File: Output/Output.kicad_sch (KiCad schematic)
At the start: 8 parts, among them J1 Conn_01x10_Pin, J2 Conn_01x04_Pin, J3 Conn_01x03_Pin, J4 Conn_01x02_Pin, J5 Conn_01x01_Pin, U2 74LS273

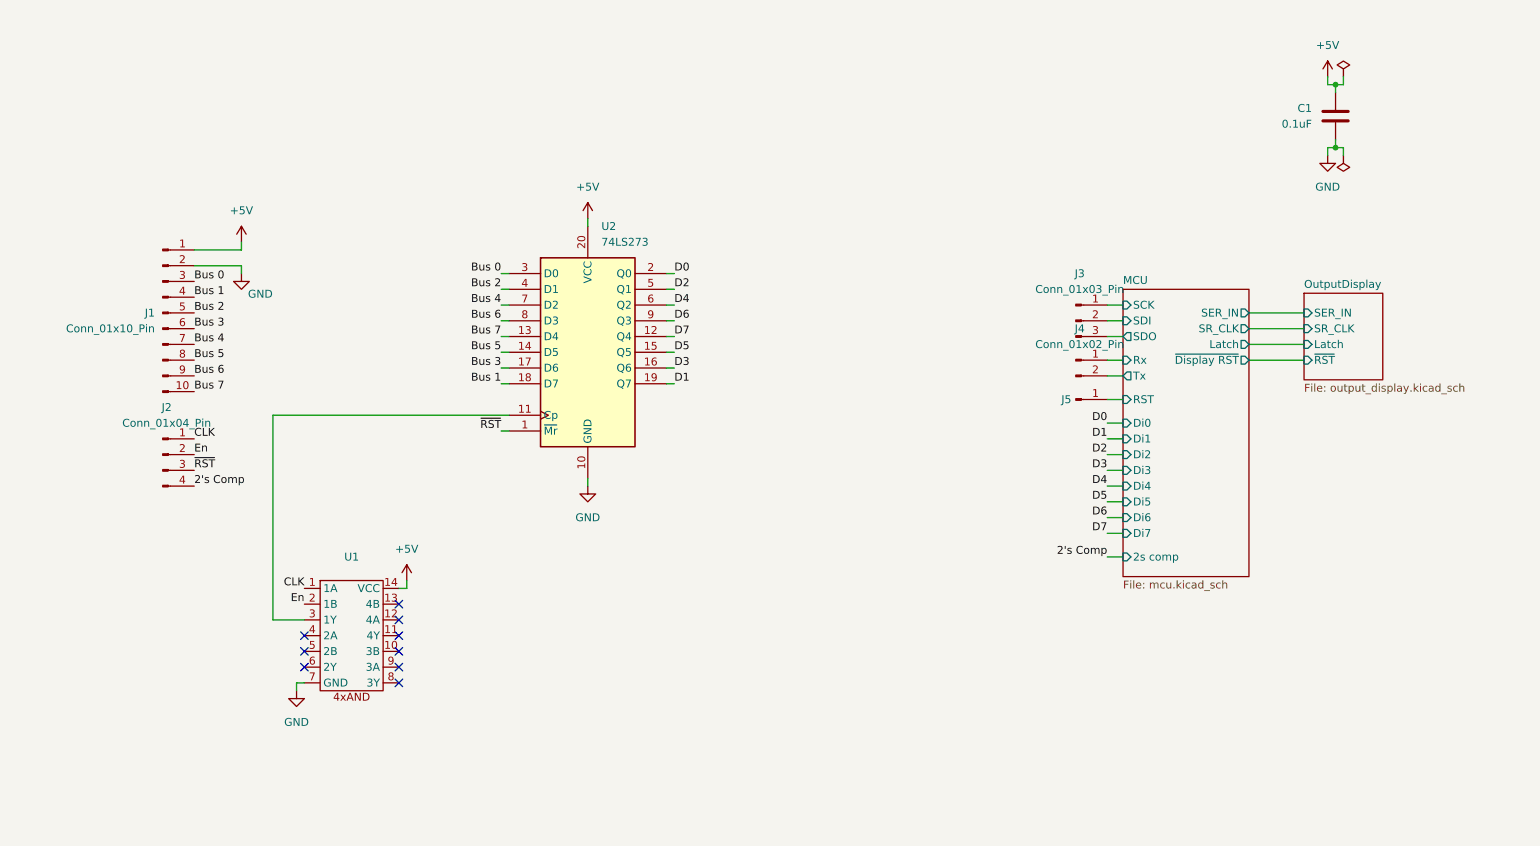
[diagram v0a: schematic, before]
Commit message: Updated output to use 2 4-bit registers instead of 1 8-bit because that's what I have. No longer need the AND for clk enable as registers have an enable pin. Enable is now active low. Reset is now active high
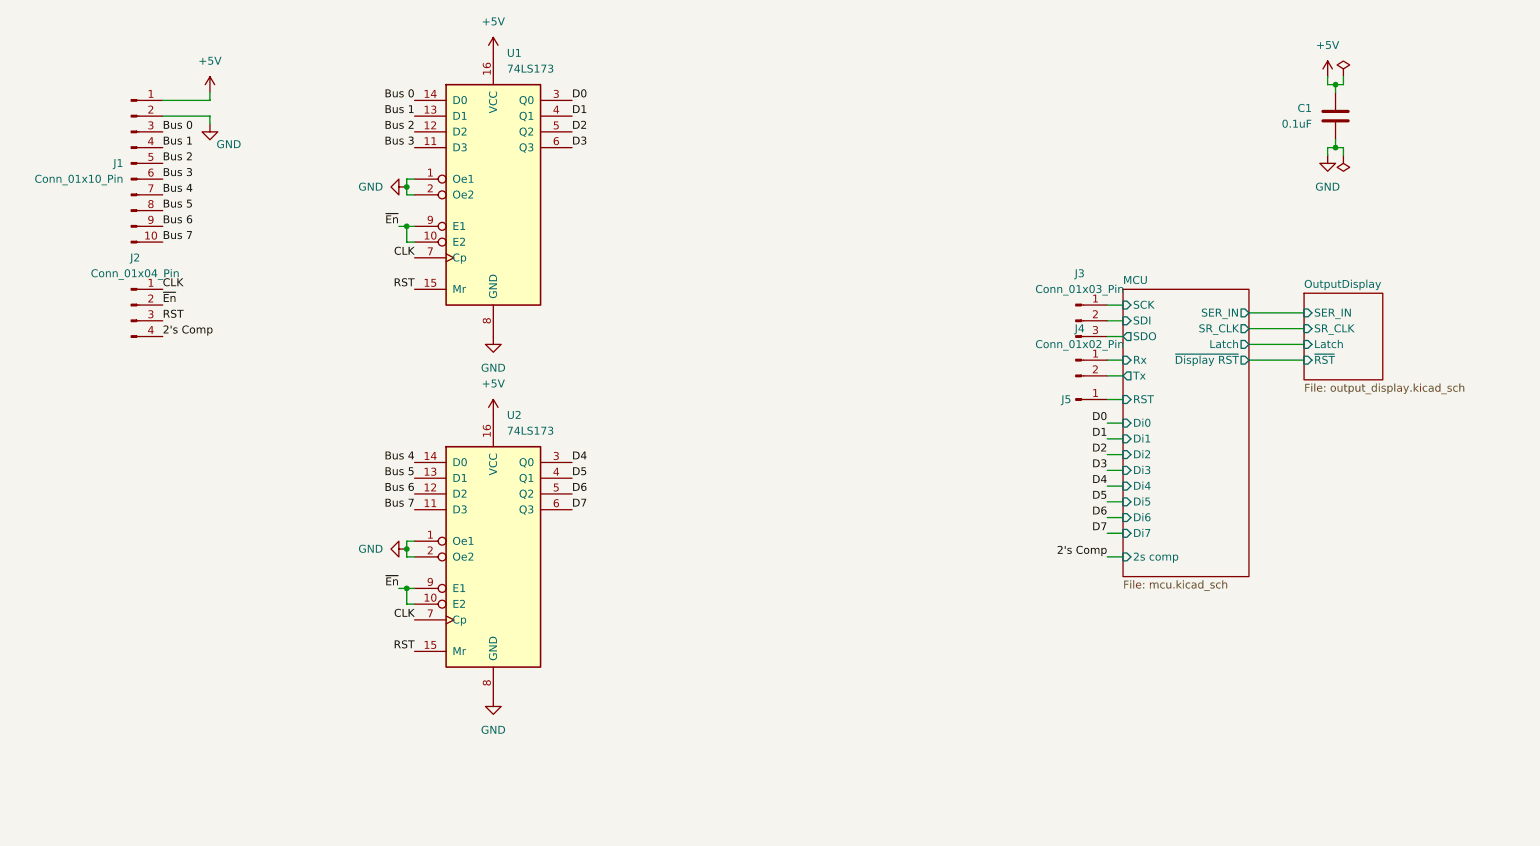
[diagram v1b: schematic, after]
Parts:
- removed U1: ~, 8BitCPUFootprints:4x_and, symbol 8BitCPU:4x_and
- removed U2: 74LS273, Package_DIP:DIP-20_W7.62mm, symbol 74xx:74LS273
- added U1, U2: 74LS173, symbol 74xx:74LS173
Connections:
- net +5V: now also U1.16 (VCC), U2.16 (VCC)
- net Bus 0: now also U1.14 (D0)
- net Bus 1: now also U1.13 (D1)
- net Bus 2: now also U1.12 (D2)
- net Bus 3: now also U1.11 (D3)
- net Bus 4: now also U2.14 (D0)
- net Bus 5: now also U2.13 (D1)
- net Bus 6: now also U2.12 (D2)
- net Bus 7: now also U2.11 (D3)
- net CLK: now also U1.7 (Cp), U2.7 (Cp)
- net D0: now also U1.3 (Q0)
- net D1: now also U1.4 (Q1)
- net D2: now also U1.5 (Q2)
- net D3: now also U1.6 (Q3)
- net D4: now also U2.3 (Q0)
- net D5: now also U2.4 (Q1)
- net D6: now also U2.5 (Q2)
- net D7: now also U2.6 (Q3)
- net GND: now also U1.1 (Oe1), U1.2 (Oe2), U1.8 (GND), U2.1 (Oe1), U2.2 (Oe2), U2.8 (GND)
- net En renamed ~{En}
- net ~{En}: now also U1.10 (E2), U1.9 (E1), U2.10 (E2), U2.9 (E1)
- net ~{RST} renamed RST
- net RST: now also U1.15 (Mr), U2.15 (Mr)
- no-connect marks 9 -> 0
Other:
- moved on the sheet: J1, J2

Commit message: Updated output to use eeprom and timing circuit instead of atmega a shift registers
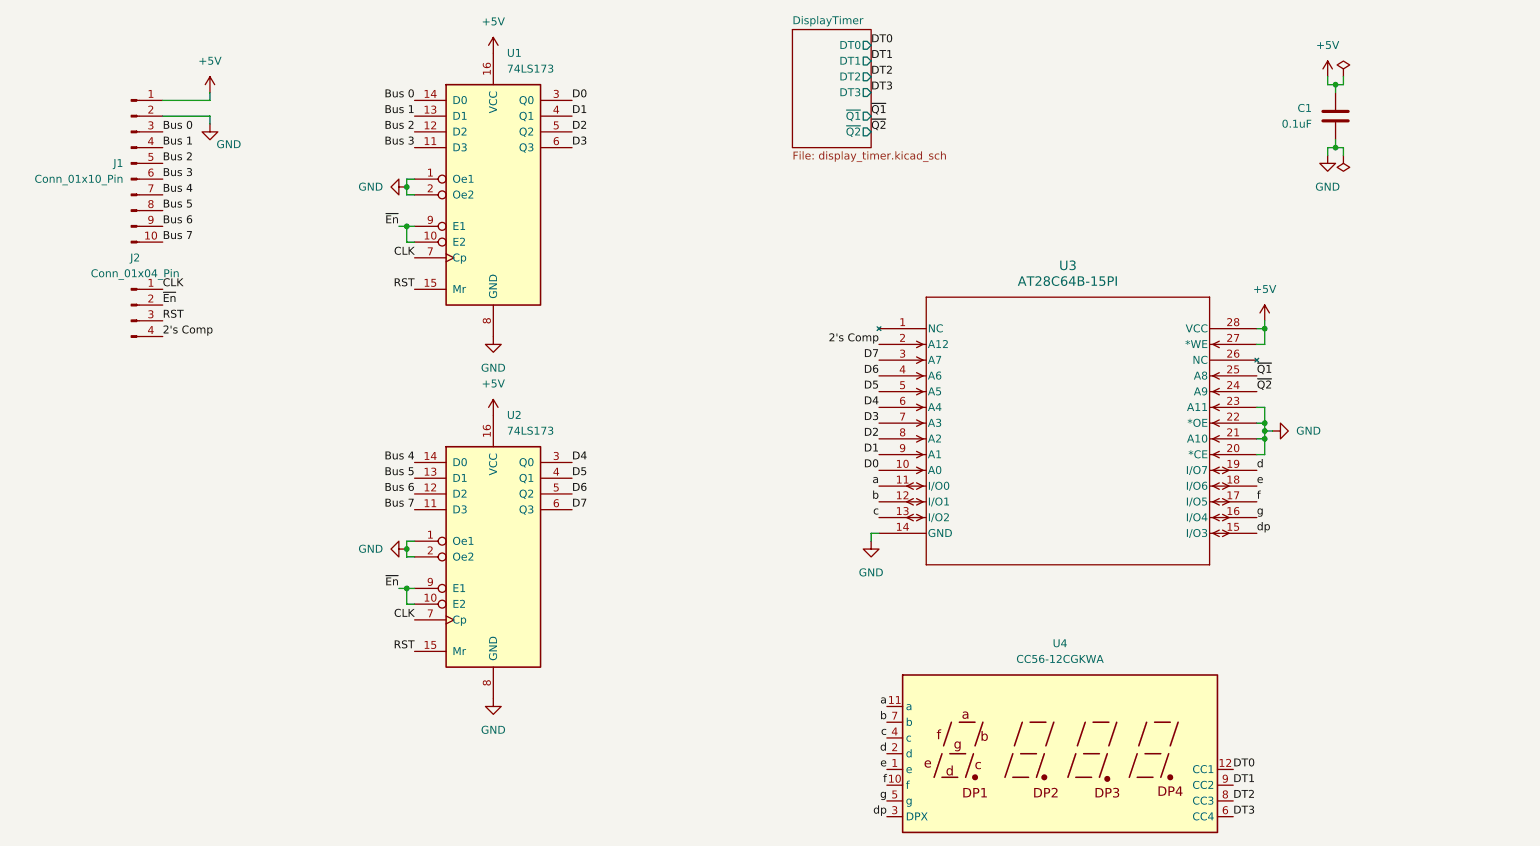
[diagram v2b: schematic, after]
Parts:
- removed J3: Conn_01x03_Pin, Connector_PinHeader_2.54mm:PinHeader_1x03_P2.54mm_Vertical, symbol Connector:Conn_01x03_Pin
- removed J4: Conn_01x02_Pin, Connector_PinHeader_2.54mm:PinHeader_1x02_P2.54mm_Vertical, symbol Connector:Conn_01x02_Pin
- removed J5: Conn_01x01_Pin, Connector_PinHeader_2.54mm:PinHeader_1x01_P2.54mm_Vertical, symbol Connector:Conn_01x01_Pin
- added U3: AT28C64B-15PI, 28P6, symbol eeprom:AT28C64B-15PI
- added U4: CC56-12CGKWA, Display_7Segment:CA56-12CGKWA, symbol Display_Character:CC56-12CGKWA
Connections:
- net +5V: now also U3.27 (*WE), U3.28 (VCC)
- net 2's Comp: now also U3.2 (A12)
- net D0: now also U3.10 (A0)
- net D1: now also U3.9 (A1)
- net D2: now also U3.8 (A2)
- net D3: now also U3.7 (A3)
- net D4: now also U3.6 (A4)
- net D5: now also U3.5 (A5)
- net D6: now also U3.4 (A6)
- net D7: now also U3.3 (A7)
- net GND: now also U3.14 (GND), U3.20 (*CE), U3.21 (A10), U3.22 (*OE), U3.23 (A11)
- new net DT0: U4.12 (CC1)
- new net DT1: U4.9 (CC2)
- new net DT2: U4.8 (CC3)
- new net DT3: U4.6 (CC4)
- new net a: U3.11 (I/O0), U4.11 (a)
- new net b: U3.12 (I/O1), U4.7 (b)
- new net c: U3.13 (I/O2), U4.4 (c)
- new net d: U3.19 (I/O7), U4.2 (d)
- new net dp: U3.15 (I/O3), U4.3 (DPX)
- new net e: U3.18 (I/O6), U4.1 (e)
- new net f: U3.17 (I/O5), U4.10 (f)
- new net g: U3.16 (I/O4), U4.5 (g)
- new net ~{Q1}: U3.25 (A8)
- new net ~{Q2}: U3.24 (A9)
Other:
- removed sheet MCU
- removed sheet OutputDisplay
- added sheet DisplayTimer (display_timer.kicad_sch)

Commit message: Output PCB routed
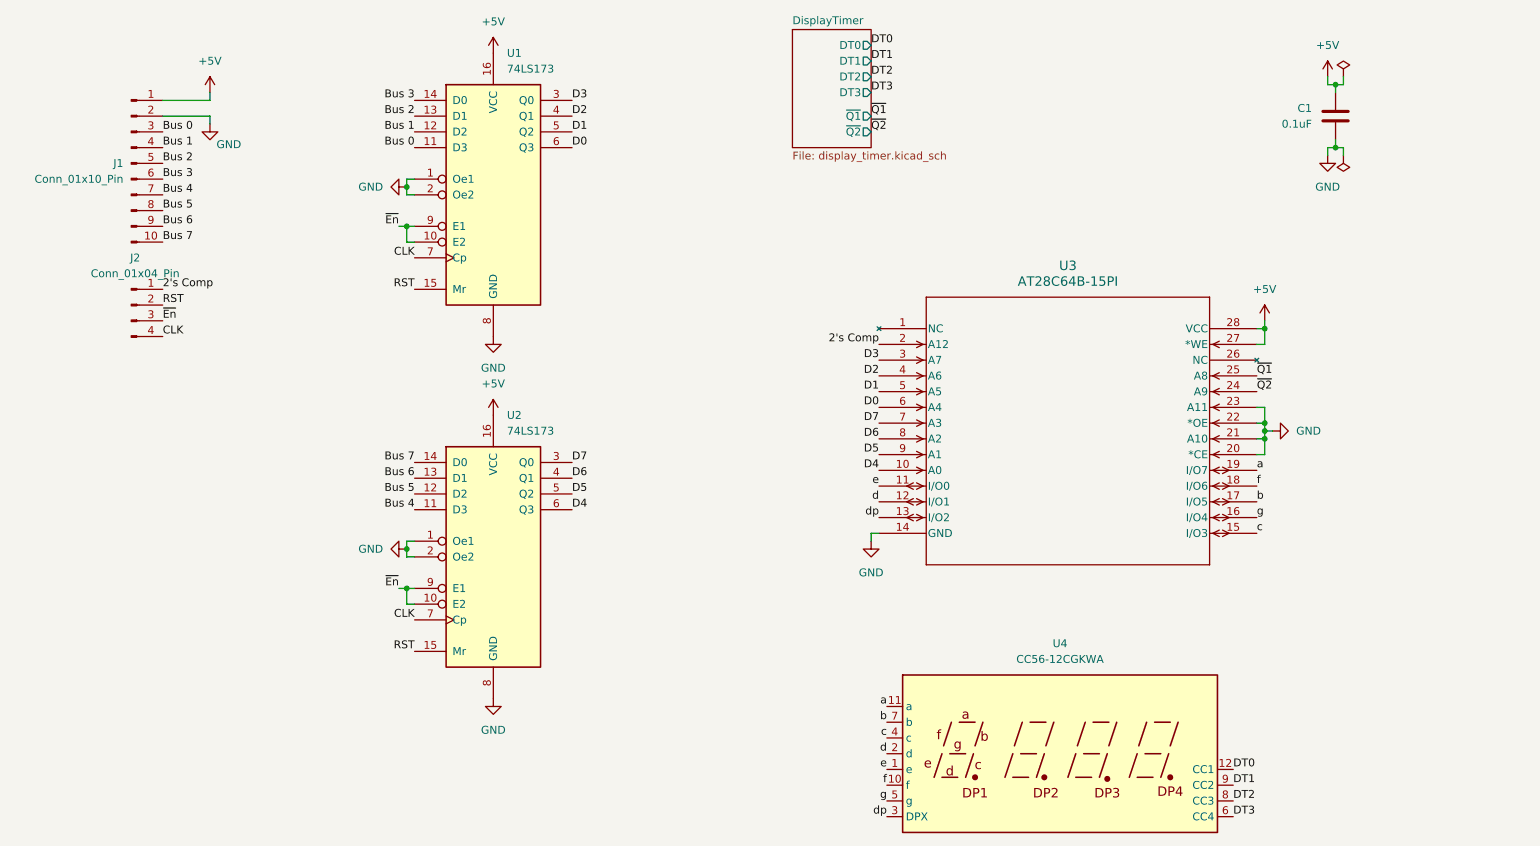
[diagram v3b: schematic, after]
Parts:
- U1, U2: footprint (none) -> Package_DIP:DIP-16_W7.62mm
- U3: footprint 28P6 -> _DownloadFootprints:eeprom
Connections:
- net 2's Comp: now also J2.1 (Pin_1); no longer J2.4 (Pin_4)
- net Bus 0: now also U1.11 (D3); no longer U1.14 (D0)
- net Bus 1: now also U1.12 (D2); no longer U1.13 (D1)
- net Bus 2: now also U1.13 (D1); no longer U1.12 (D2)
- net Bus 3: now also U1.14 (D0); no longer U1.11 (D3)
- net Bus 4: now also U2.11 (D3); no longer U2.14 (D0)
- net Bus 5: now also U2.12 (D2); no longer U2.13 (D1)
- net Bus 6: now also U2.13 (D1); no longer U2.12 (D2)
- net Bus 7: now also U2.14 (D0); no longer U2.11 (D3)
- net CLK: now also J2.4 (Pin_4); no longer J2.1 (Pin_1)
- net D0: now also U1.6 (Q3), U3.6 (A4); no longer U1.3 (Q0), U3.10 (A0)
- net D1: now also U1.5 (Q2), U3.5 (A5); no longer U1.4 (Q1), U3.9 (A1)
- net D2: now also U1.4 (Q1), U3.4 (A6); no longer U1.5 (Q2), U3.8 (A2)
- net D3: now also U1.3 (Q0), U3.3 (A7); no longer U1.6 (Q3), U3.7 (A3)
- net D4: now also U2.6 (Q3), U3.10 (A0); no longer U2.3 (Q0), U3.6 (A4)
- net D5: now also U2.5 (Q2), U3.9 (A1); no longer U2.4 (Q1), U3.5 (A5)
- net D6: now also U2.4 (Q1), U3.8 (A2); no longer U2.5 (Q2), U3.4 (A6)
- net D7: now also U2.3 (Q0), U3.7 (A3); no longer U2.6 (Q3), U3.3 (A7)
- net RST: now also J2.2 (Pin_2); no longer J2.3 (Pin_3)
- net a: now also U3.19 (I/O7); no longer U3.11 (I/O0)
- net b: now also U3.17 (I/O5); no longer U3.12 (I/O1)
- net c: now also U3.15 (I/O3); no longer U3.13 (I/O2)
- net d: now also U3.12 (I/O1); no longer U3.19 (I/O7)
- net dp: now also U3.13 (I/O2); no longer U3.15 (I/O3)
- net e: now also U3.11 (I/O0); no longer U3.18 (I/O6)
- net f: now also U3.18 (I/O6); no longer U3.17 (I/O5)
- net ~{En}: now also J2.3 (Pin_3); no longer J2.2 (Pin_2)
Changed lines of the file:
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@@
 	)
 	(label "D1"
-		(at 107.95 35.56 0)
+		(at 107.95 38.1 0)
 		(fields_autoplaced yes)
 		(effects
@@
 	)
 	(label "D5"
-		(at 157.48 80.01 180)
+		(at 157.48 90.17 180)
 		(fields_autoplaced yes)
 		(effects
@@
 	)
 	(label "dp"
-		(at 218.44 102.87 0)
-		(fields_autoplaced yes)
-		(effects
-			(font
-				(size 1.27 1.27)
-			)
-			(justify left bottom)
+		(at 157.48 100.33 180)
+		(fields_autoplaced yes)
+		(effects
+			(font
+				(size 1.27 1.27)
+			)
+			(justify right bottom)
 		)
 	)
@@
 	)
 	(label "e"
-		(at 218.44 95.25 0)
-		(fields_autoplaced yes)
-		(effects
-			(font
-				(size 1.27 1.27)
-			)
-			(justify left bottom)
+		(at 157.48 95.25 180)
+		(fields_autoplaced yes)
+		(effects
+			(font
+				(size 1.27 1.27)
+			)
+			(justify right bottom)
 		)
 	)
@@
 	)
 	(label "D6"
-		(at 107.95 96.52 0)
+		(at 107.95 93.98 0)
 		(fields_autoplaced yes)
 		(effects
@@
 	)
 	(label "CLK"
-		(at 41.91 63.5 0)
+		(at 41.91 71.12 0)
 		(fields_autoplaced yes)
 		(effects
@@
 	)
 	(label "D4"
-		(at 107.95 91.44 0)
+		(at 107.95 99.06 0)
 		(fields_autoplaced yes)
 		(effects
@@
 	)
 	(label "d"
-		(at 218.44 92.71 0)
-		(fields_autoplaced yes)
-		(effects
-			(font
-				(size 1.27 1.27)
-			)
-			(justify left bottom)
+		(at 157.48 97.79 180)
+		(fields_autoplaced yes)
+		(effects
+			(font
+				(size 1.27 1.27)
+			)
+			(justify right bottom)
 		)
 	)
 	(label "D3"
-		(at 107.95 40.64 0)
+		(at 107.95 33.02 0)
 		(fields_autoplaced yes)
 		(effects
@@
 	)
 	(label "f"
-		(at 218.44 97.79 0)
+		(at 218.44 95.25 0)
 		(fields_autoplaced yes)
 		(effects
@@
 	)
 	(label "D2"
-		(at 157.48 87.63 180)
+		(at 157.48 77.47 180)
 		(fields_autoplaced yes)
 		(effects
@@
 	)
 	(label "Bus 5"
-		(at 82.55 93.98 180)
+		(at 82.55 96.52 180)
 		(fields_autoplaced yes)
 		(effects
@@
 	)
 	(label "RST"
-		(at 41.91 68.58 0)
+		(at 41.91 66.04 0)
 		(fields_autoplaced yes)
 		(effects
@@
 	)
 	(label "D2"
-		(at 107.95 38.1 0)
+		(at 107.95 35.56 0)
 		(fields_autoplaced yes)
 		(effects
@@
 	)
 	(label "D4"
-		(at 157.48 82.55 180)
+		(at 157.48 92.71 180)
 		(fields_autoplaced yes)
 		(effects
@@
 	)
 	(label "c"
-		(at 157.48 100.33 180)
-		(fields_autoplaced yes)
-		(effects
-			(font
-				(size 1.27 1.27)
-			)
-			(justify right bottom)
+		(at 218.44 102.87 0)
+		(fields_autoplaced yes)
+		(effects
+			(font
+				(size 1.27 1.27)
+			)
+			(justify left bottom)
 		)
 	)
 	(label "b"
-		(at 157.48 97.79 180)
-		(fields_autoplaced yes)
-		(effects
-			(font
-				(size 1.27 1.27)
-			)
-			(justify right bottom)
+		(at 218.44 97.79 0)
+		(fields_autoplaced yes)
+		(effects
+			(font
+				(size 1.27 1.27)
+			)
+			(justify left bottom)
 		)
 	)
 	(label "D6"
-		(at 157.48 77.47 180)
+		(at 157.48 87.63 180)
 		(fields_autoplaced yes)
 		(effects
@@
 	)
 	(label "2's Comp"
-		(at 41.91 71.12 0)
+		(at 41.91 63.5 0)
 		(fields_autoplaced yes)
 		(effects
@@
 	)
 	(label "Bus 7"
-		(at 82.55 99.06 180)
+		(at 82.55 91.44 180)
 		(fields_autoplaced yes)
 		(effects
@@
 	)
 	(label "~{En}"
-		(at 41.91 66.04 0)
+		(at 41.91 68.58 0)
 		(fields_autoplaced yes)
 		(effects
@@
 	)
 	(label "D1"
-		(at 157.48 90.17 180)
+		(at 157.48 80.01 180)
 		(fields_autoplaced yes)
 		(effects
@@
 	)
 	(label "D7"
-		(at 107.95 99.06 0)
+		(at 107.95 91.44 0)
 		(fields_autoplaced yes)
 		(effects
@@
 	)
 	(label "D3"
-		(at 157.48 85.09 180)
+		(at 157.48 74.93 180)
 		(fields_autoplaced yes)
 		(effects
@@
 	)
 	(label "Bus 2"
-		(at 82.55 38.1 180)
+		(at 82.55 35.56 180)
 		(fields_autoplaced yes)
 		(effects
@@
 	)
 	(label "Bus 3"
-		(at 82.55 40.64 180)
+		(at 82.55 33.02 180)
 		(fields_autoplaced yes)
 		(effects
@@
 	)
 	(label "Bus 1"
-		(at 82.55 35.56 180)
+		(at 82.55 38.1 180)
 		(fields_autoplaced yes)
 		(effects
@@
 	)
 	(label "Bus 6"
-		(at 82.55 96.52 180)
+		(at 82.55 93.98 180)
 		(fields_autoplaced yes)
 		(effects
@@
 	)
 	(label "D5"
-		(at 107.95 93.98 0)
+		(at 107.95 96.52 0)
 		(fields_autoplaced yes)
 		(effects
@@
 	)
 	(label "D0"
-		(at 157.48 92.71 180)
+		(at 157.48 82.55 180)
 		(fields_autoplaced yes)
 		(effects
@@
 	)
 	(label "D7"
-		(at 157.48 74.93 180)
+		(at 157.48 85.09 180)
 		(fields_autoplaced yes)
 		(effects
@@
 	)
 	(label "a"
-		(at 157.48 95.25 180)
-		(fields_autoplaced yes)
-		(effects
-			(font
-				(size 1.27 1.27)
-			)
-			(justify right bottom)
+		(at 218.44 92.71 0)
+		(fields_autoplaced yes)
+		(effects
+			(font
+				(size 1.27 1.27)
+			)
+			(justify left bottom)
 		)
 	)
@@
 	)
 	(label "Bus 4"
-		(at 82.55 91.44 180)
+		(at 82.55 99.06 180)
 		(fields_autoplaced yes)
 		(effects
@@
 	)
 	(label "D0"
-		(at 107.95 33.02 0)
+		(at 107.95 40.64 0)
 		(fields_autoplaced yes)
 		(effects
@@
 	)
 	(label "Bus 0"
-		(at 82.55 33.02 180)
+		(at 82.55 40.64 180)
 		(fields_autoplaced yes)
 		(effects
@@
 			)
 		)
-		(property "Footprint" ""
+		(property "Footprint" "Package_DIP:DIP-16_W7.62mm"
 			(at 95.25 106.68 0)
 			(effects
@@
 			)
 		)
-		(property "Footprint" ""
+		(property "Footprint" "Package_DIP:DIP-16_W7.62mm"
 			(at 95.25 48.26 0)
 			(effects
@@
 			)
 		)
-		(property "Footprint" "28P6"
+		(property "Footprint" "_DownloadFootprints:eeprom"
 			(at 157.48 69.85 0)
 			(effects
